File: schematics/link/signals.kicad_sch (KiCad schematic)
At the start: 39 parts, among them SW1 Feedbacks, SW2 Returns, SW3 Feedbacks, SW4 Returns, U4 AD8422ARMZ, U5 OPA2182, U6 AD8422ARMZ

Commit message: update(pcb): combining modules
Want to try a different layout, but like where I am at right now
Planning to branch off of this one and see where it goes
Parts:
- C15, C16, C17, C18, C19, C20, C21, C22, C23, C24: footprint Capacitor_SMD:C_0603_1608Metric -> Capacitor_SMD:C_0402_1005Metric
- R10, R11, R13, R14, R16, R17, R20, R21, R23, R24, R26, R27: footprint Resistor_SMD:R_0603_1608Metric -> Resistor_SMD:R_0402_1005Metric
- R12, R15, R22, R25: footprint Resistor_SMD:R_0603_1608Metric -> Resistor_SMD:R_0402_1005Metric_Pad0.72x0.64mm_HandSolder
- TP10, TP11: footprint TestPoint:TestPoint_Pad_D1.0mm -> Link_Footprints:TestPoint_Pad_D1.5mm
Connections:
- net GND: now also U5.3 (+), U5.5 (+); no longer U5.3 (+), U5.5 (+)
- net Sc1-: now also U5.7; no longer U5.1
- net Sc2-: now also U5.1; no longer U5.7
- net at C21.1, R27.2: now also U5.2 (-); no longer U5.6 (-)
- net at C22.2, R23.2, R24.2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: no longer TP11.1
- net at C18.2, R13.2, R14.2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: no longer TP10.1
- net at C17.1, R17.2: now also U5.6 (-); no longer U5.2 (-)
- net at SW3.1, SW3.2, SW3.3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: now also TP11.1
- net at SW1.1, SW1.2, SW1.3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: now also TP10.1
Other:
- moved on the sheet: TP10, TP11
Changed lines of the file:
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@@
 	)
 	(junction
-		(at 137.16 53.34)
+		(at 85.09 53.34)
 		(diameter 0)
 		(color 0 0 0 0)
 	)
 	(junction
-		(at 128.27 116.84)
+		(at 137.16 53.34)
 		(diameter 0)
 		(color 0 0 0 0)
 	)
 	(junction
-		(at 128.27 50.8)
+		(at 128.27 116.84)
 		(diameter 0)
 		(color 0 0 0 0)
@@
 	)
 	(junction
-		(at 128.27 114.3)
+		(at 92.71 53.34)
 		(diameter 0)
 		(color 0 0 0 0)
 	)
 	(junction
-		(at 92.71 53.34)
+		(at 137.16 116.84)
 		(diameter 0)
 		(color 0 0 0 0)
 	)
 	(junction
-		(at 137.16 116.84)
+		(at 85.09 116.84)
 		(diameter 0)
 		(color 0 0 0 0)
@@
 	(wire
 		(pts
+			(xy 85.09 116.84) (xy 92.71 116.84)
+		)
+		(stroke
+			(width 0)
+			(type default)
+		)
+	)
+	(wire
+		(pts
 			(xy 40.64 77.47) (xy 40.64 80.01)
 		)
@@
 	(wire
 		(pts
-			(xy 83.82 53.34) (xy 92.71 53.34)
+			(xy 83.82 53.34) (xy 85.09 53.34)
 		)
 		(stroke
@@
 	(wire
 		(pts
+			(xy 85.09 53.34) (xy 92.71 53.34)
+		)
+		(stroke
+			(width 0)
+			(type default)
+		)
+	)
+	(wire
+		(pts
 			(xy 241.3 45.72) (xy 247.65 45.72)
 		)
@@
 	(wire
 		(pts
-			(xy 83.82 116.84) (xy 92.71 116.84)
+			(xy 83.82 116.84) (xy 85.09 116.84)
 		)
 		(stroke
@@
 			)
 		)
-		(property "Footprint" "Capacitor_SMD:C_0603_1608Metric"
+		(property "Footprint" "Capacitor_SMD:C_0402_1005Metric"
 			(at 241.3 67.31 0)
 			(hide yes)
@@
 			)
 		)
-		(property "Footprint" "Resistor_SMD:R_0603_1608Metric"
+		(property "Footprint" "Resistor_SMD:R_0402_1005Metric_Pad0.72x0.64mm_HandSolder"
 			(at 60.96 116.84 0)
 			(hide yes)
@@
 		(at 156.21 119.38 0)
 		(mirror x)
-		(unit 2)
+		(unit 1)
 		(body_style 1)
 		(exclude_from_sim no)
@@
 				(path "/e6a73b1b-9233-47b9-8d6b-253608bed688/8a1af58c-1394-41ad-9137-7f60a6d007c9"
 					(reference "U5")
-					(unit 2)
+					(unit 1)
 				)
 			)
@@
 	(symbol
 		(lib_id "Connector:TestPoint")
-		(at 128.27 114.3 0)
+		(at 85.09 116.84 180)
 		(unit 1)
 		(body_style 1)
@@
 		(dnp no)
 		(property "Reference" "TP11"
-			(at 128.27 108.204 0)
+			(at 85.09 122.936 0)
 			(show_name no)
 			(do_not_autoplace no)
@@
 		)
 		(property "Value" "S2"
-			(at 128.27 106.426 0)
+			(at 85.09 124.714 0)
 			(show_name no)
 			(do_not_autoplace no)
@@
 			)
 		)
-		(property "Footprint" "TestPoint:TestPoint_Pad_D1.0mm"
-			(at 133.35 114.3 0)
+		(property "Footprint" "Link_Footprints:TestPoint_Pad_D1.5mm"
+			(at 80.01 116.84 0)
 			(hide yes)
 			(show_name no)
@@
 		)
 		(property "Datasheet" ""
-			(at 133.35 114.3 0)
+			(at 80.01 116.84 0)
 			(hide yes)
 			(show_name no)
@@
 		)
 		(property "Description" "test point"
-			(at 128.27 114.3 0)
+			(at 85.09 116.84 0)
 			(hide yes)
 			(show_name no)
@@
 		)
 		(property "FT Rotation Offset" ""
-			(at 128.27 114.3 0)
+			(at 85.09 116.84 0)
 			(hide yes)
 			(show_name no)
@@
 		)
 		(property "Sim.Params" ""
-			(at 128.27 114.3 0)
+			(at 85.09 116.84 0)
 			(hide yes)
 			(show_name no)
@@
 			)
 		)
-		(property "Footprint" "Resistor_SMD:R_0603_1608Metric"
+		(property "Footprint" "Resistor_SMD:R_0402_1005Metric"
 			(at 113.03 50.8 0)
 			(hide yes)
@@
 			)
 		)
-		(property "Footprint" "Capacitor_SMD:C_0603_1608Metric"
+		(property "Footprint" "Capacitor_SMD:C_0402_1005Metric"
 			(at 241.3 49.53 0)
 			(hide yes)
@@
 			)
 		)
-		(property "Footprint" "Resistor_SMD:R_0603_1608Metric"
+		(property "Footprint" "Resistor_SMD:R_0402_1005Metric"
 			(at 142.24 53.34 0)
 			(hide yes)
@@
 			)
 		)
-		(property "Footprint" "Capacitor_SMD:C_0603_1608Metric"
+		(property "Footprint" "Capacitor_SMD:C_0402_1005Metric"
 			(at 67.31 38.1 0)
 			(hide yes)
@@
 			)
 		)
-		(property "Footprint" "Resistor_SMD:R_0603_1608Metric"
+		(property "Footprint" "Resistor_SMD:R_0402_1005Metric"
 			(at 142.24 116.84 0)
 			(hide yes)
@@
 			)
 		)
-		(property "Footprint" "Capacitor_SMD:C_0603_1608Metric"
+		(property "Footprint" "Capacitor_SMD:C_0402_1005Metric"
 			(at 64.77 66.04 0)
 			(hide yes)
@@
 			)
 		)
-		(property "Footprint" "Resistor_SMD:R_0603_1608Metric"
+		(property "Footprint" "Resistor_SMD:R_0402_1005Metric"
 			(at 113.03 53.34 0)
 			(hide yes)
@@
 			)
 		)
-		(property "Footprint" "Resistor_SMD:R_0603_1608Metric"
+		(property "Footprint" "Resistor_SMD:R_0402_1005Metric_Pad0.72x0.64mm_HandSolder"
 			(at 60.96 53.34 0)
 			(hide yes)
@@
 	(symbol
 		(lib_id "Connector:TestPoint")
-		(at 128.27 50.8 0)
+		(at 85.09 53.34 180)
 		(unit 1)
 		(body_style 1)
@@
 		(dnp no)
 		(property "Reference" "TP10"
-			(at 128.27 44.704 0)
+			(at 85.09 59.436 0)
 			(show_name no)
 			(do_not_autoplace no)
@@
 		)
 		(property "Value" "S1"
-			(at 128.27 42.926 0)
+			(at 85.09 61.214 0)
 			(show_name no)
 			(do_not_autoplace no)
@@
 			)
 		)
-		(property "Footprint" "TestPoint:TestPoint_Pad_D1.0mm"
-			(at 133.35 50.8 0)
+		(property "Footprint" "Link_Footprints:TestPoint_Pad_D1.5mm"
+			(at 80.01 53.34 0)
 			(hide yes)
 			(show_name no)
@@
 		)
 		(property "Datasheet" ""
-			(at 133.35 50.8 0)
+			(at 80.01 53.34 0)
 			(hide yes)
 			(show_name no)
@@
 		)
 		(property "Description" "test point"
-			(at 128.27 50.8 0)
+			(at 85.09 53.34 0)
 			(hide yes)
 			(show_name no)
@@
 		)
 		(property "FT Rotation Offset" ""
-			(at 128.27 50.8 0)
+			(at 85.09 53.34 0)
 			(hide yes)
 			(show_name no)
@@
 		)
 		(property "Sim.Params" ""
-			(at 128.27 50.8 0)
+			(at 85.09 53.34 0)
 			(hide yes)
 			(show_name no)
@@
 			)
 		)
-		(property "Footprint" "Capacitor_SMD:C_0603_1608Metric"
+		(property "Footprint" "Capacitor_SMD:C_0402_1005Metric"
 			(at 64.77 129.54 0)
 			(hide yes)
@@
 			)
 		)
-		(property "Footprint" "Resistor_SMD:R_0603_1608Metric"
+		(property "Footprint" "Resistor_SMD:R_0402_1005Metric"
 			(at 113.03 116.84 0)
 			(hide yes)
@@
 		(at 156.21 55.88 0)
 		(mirror x)
-		(unit 1)
+		(unit 2)
 		(body_style 1)
 		(exclude_from_sim no)
@@
 				(path "/e6a73b1b-9233-47b9-8d6b-253608bed688/8a1af58c-1394-41ad-9137-7f60a6d007c9"
 					(reference "U5")
-					(unit 1)
+					(unit 2)
 				)
 			)
@@
 			)
 		)
-		(property "Footprint" "Capacitor_SMD:C_0603_1608Metric"
+		(property "Footprint" "Capacitor_SMD:C_0402_1005Metric"
 			(at 137.16 121.92 0)
 			(hide yes)
@@
 			)
 		)
-		(property "Footprint" "Resistor_SMD:R_0603_1608Metric"
+		(property "Footprint" "Resistor_SMD:R_0402_1005Metric"
 			(at 154.94 33.02 0)
 			(hide yes)
@@
 			)
 		)
-		(property "Footprint" "Capacitor_SMD:C_0603_1608Metric"
+		(property "Footprint" "Capacitor_SMD:C_0402_1005Metric"
 			(at 154.94 106.68 0)
 			(hide yes)
@@
 			)
 		)
-		(property "Footprint" "Resistor_SMD:R_0603_1608Metric"
+		(property "Footprint" "Resistor_SMD:R_0402_1005Metric_Pad0.72x0.64mm_HandSolder"
 			(at 113.03 55.88 0)
 			(hide yes)
@@
 			)
 		)
-		(property "Footprint" "Capacitor_SMD:C_0603_1608Metric"
+		(property "Footprint" "Capacitor_SMD:C_0402_1005Metric"
 			(at 154.94 43.18 0)
 			(hide yes)
@@
 			)
 		)
-		(property "Footprint" "Resistor_SMD:R_0603_1608Metric"
+		(property "Footprint" "Resistor_SMD:R_0402_1005Metric"
 			(at 24.13 48.26 0)
 			(hide yes)
@@
 			)
 		)
-		(property "Footprint" "Resistor_SMD:R_0603_1608Metric"
+		(property "Footprint" "Resistor_SMD:R_0402_1005Metric"
 			(at 154.94 96.52 0)
 			(hide yes)
@@
 			)
 		)
-		(property "Footprint" "Resistor_SMD:R_0603_1608Metric"
+		(property "Footprint" "Resistor_SMD:R_0402_1005Metric"
 			(at 24.13 58.42 0)
 			(hide yes)
@@
 			)
 		)
-		(property "Footprint" "Resistor_SMD:R_0603_1608Metric"
+		(property "Footprint" "Resistor_SMD:R_0402_1005Metric_Pad0.72x0.64mm_HandSolder"
 			(at 113.03 119.38 0)
 			(hide yes)
@@
 			)
 		)
-		(property "Footprint" "Resistor_SMD:R_0603_1608Metric"
+		(property "Footprint" "Resistor_SMD:R_0402_1005Metric"
 			(at 24.13 111.76 0)
 			(hide yes)
@@
 			)
 		)
-		(property "Footprint" "Resistor_SMD:R_0603_1608Metric"
+		(property "Footprint" "Resistor_SMD:R_0402_1005Metric"
 			(at 24.13 121.92 0)
 			(hide yes)
@@
 			)
 		)
-		(property "Footprint" "Resistor_SMD:R_0603_1608Metric"
+		(property "Footprint" "Resistor_SMD:R_0402_1005Metric"
 			(at 113.03 114.3 0)
 			(hide yes)
@@
 			)
 		)
-		(property "Footprint" "Capacitor_SMD:C_0603_1608Metric"
+		(property "Footprint" "Capacitor_SMD:C_0402_1005Metric"
 			(at 137.16 58.42 0)
 			(hide yes)
@@
 			)
 		)
-		(property "Footprint" "Capacitor_SMD:C_0603_1608Metric"
+		(property "Footprint" "Capacitor_SMD:C_0402_1005Metric"
 			(at 67.31 101.6 0)
 			(hide yes)

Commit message: update(link): finalized placements
Still some work to be done:
1. Fix planes under RJ45 connector, probably should keep out if possible
2. Fix silkscreening
3. Fix isolated filled zones
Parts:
- TP10: value S1 -> S2
- TP11: value S2 -> S1
- renumbered C15 to C17, C17 to C18, C23 to C19, C18 to C20, C16 to C21, C24 to C22, C19 to C23, C21 to C24, C22 to C25, C20 to C26, R16 to R10, R10 to R11, R13 to R12, R12 to R13, R17 to R15, R15 to R16, R11 to R17, R26 to R20, R20 to R21, R23 to R22, R22 to R23, R27 to R25, R25 to R26, R21 to R27
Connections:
- net S1+: now also R27.1; no longer R17.1
- net S1-: now also R21.1; no longer R11.1
- net S2+: now also R17.1; no longer R27.1
- net S2-: now also R11.1; no longer R21.1
- net Sc1-: now also C24.2, R20.2, U5.1; no longer C18.2, R10.2, U5.7
- net Sc2-: now also C18.2, R10.2, U5.7; no longer C24.2, R20.2, U5.1

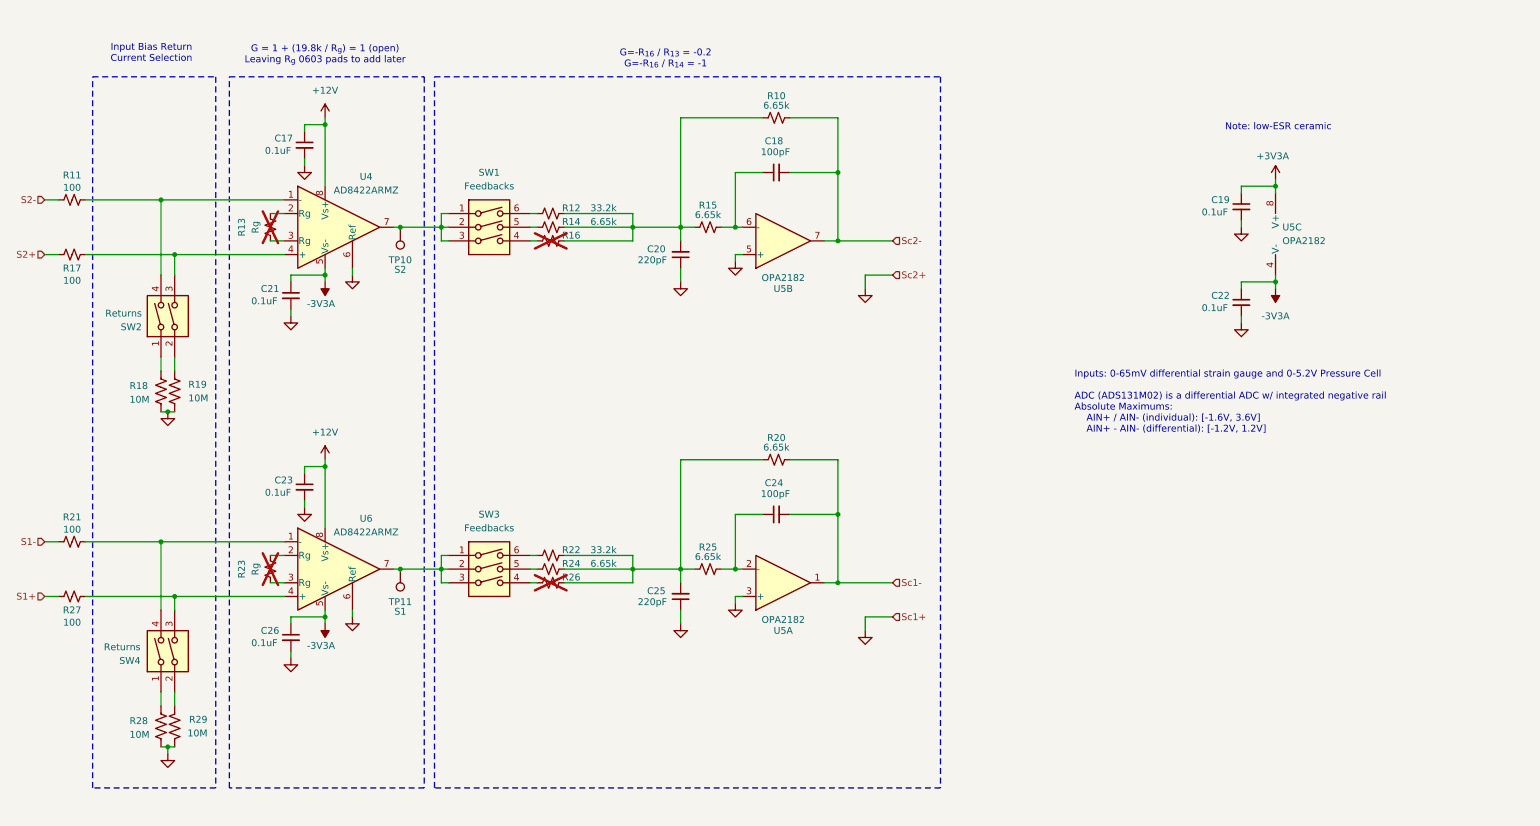
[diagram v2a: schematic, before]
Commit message: update(review):
1. Take gain resistor out of AFE filter
2. Breakout I2C
3. Move fuse to cover both 12V rails
4. Silkscreens
5. More testpoints + change to clip ons
6. Match ADC input max and filter output max
7. Add shunt for current resistors
8. Thermocouples
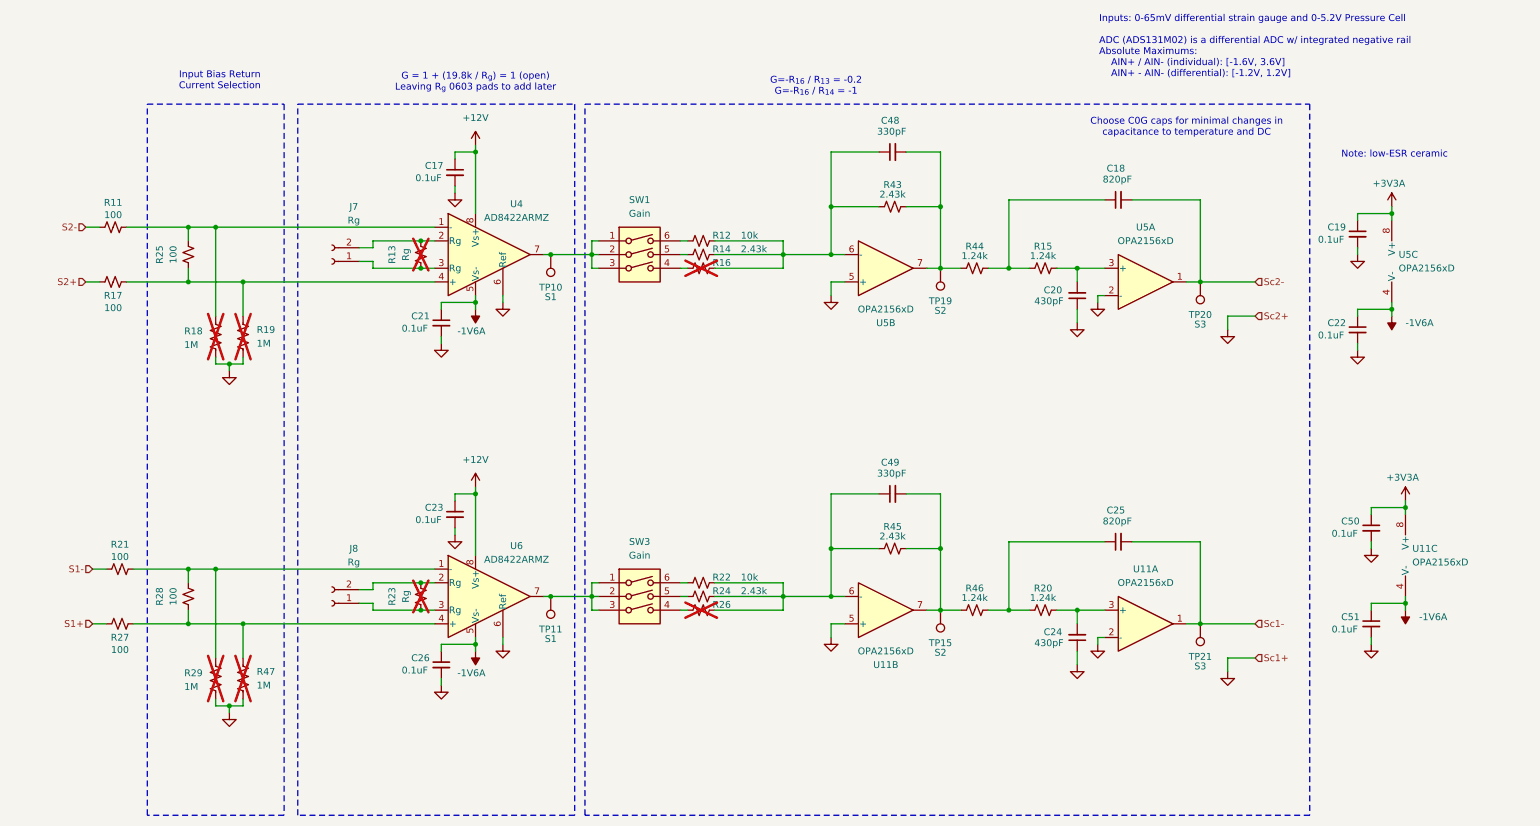
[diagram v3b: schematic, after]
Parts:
- removed R10: 6.65k, Resistor_SMD:R_0402_1005Metric, symbol Device:R_Small_US
- removed R28: 10M, Resistor_SMD:R_0603_1608Metric, symbol Device:R_US
- removed SW2, SW4: Returns, Button_Switch_SMD:SW_DIP_SPSTx02_Slide_KingTek_DSHP02TJ_W5.25mm_P1.27mm_JPin, symbol Switch:SW_DIP_x02
- removed U5: OPA2182, Link_Footprints:OPA2182, symbol Link_Components:OPA2182
- added C48, C49: 330pF, Capacitor_SMD:C_0402_1005Metric, symbol Device:C_Small
- added C50, C51: 0.1uF, Capacitor_SMD:C_0402_1005Metric, symbol Device:C_Small
- added J7, J8: Rg, Connector_PinSocket_2.54mm:PinSocket_1x02_P2.54mm_Vertical, symbol Connector:Conn_01x02_Socket
- added R28: 100, Connector_PinSocket_2.54mm:PinSocket_1x02_P2.54mm_Vertical, symbol Device:R_Small_US
- added R43, R45: 2.43k, Resistor_SMD:R_0402_1005Metric, symbol Device:R_Small_US
- added R44, R46: 1.24k, Resistor_SMD:R_0402_1005Metric, symbol Device:R_Small_US
- added R47: 1M, Resistor_SMD:R_0603_1608Metric_Pad0.98x0.95mm_HandSolder, symbol Device:R_US
- added TP15, TP19: S2, Link_Footprints:Keystone5001, symbol Connector:TestPoint
- added TP20, TP21: S3, Link_Footprints:Keystone5001, symbol Connector:TestPoint
- added U11, U5: OPA2156xD, Package_SO:SOIC-8_3.9x4.9mm_P1.27mm, symbol Amplifier_Operational:OPA2156xD
- C17, C19, C21, C22, C23, C26: MPN (none) -> GRM155R71H104KE14D
- C18: value 100pF -> 820pF; MPN (none) -> GRM1555C1H821JA01D
- C20: value 220pF -> 430pF; MPN (none) -> GCM1555C1H431FA16D
- C24: value 100pF -> 430pF; MPN (none) -> GCM1555C1H431FA16D
- C25: value 220pF -> 820pF; MPN (none) -> GRM1555C1H821JA01D
- R11, R17, R21, R27: MPN (none) -> RT0402BRD07100RL
- R12, R22: value 33.2k -> 10k; MPN (none) -> RT0402BRD0710KL
- R13, R23: MPN (none) -> N/A
- R14, R24: value 6.65k -> 2.43k; MPN (none) -> RT0402FRE072K43L
- R15, R20: value 6.65k -> 1.24k; MPN (none) -> RT0402BRD071K24L
- R16, R26: MPN (none) -> N/A; now left out of the parts list
- R18, R19: value 10M -> 1M; footprint Resistor_SMD:R_0603_1608Metric -> Resistor_SMD:R_0603_1608Metric_Pad0.98x0.95mm_HandSolder; MPN (none) -> RC0603FR-071ML; now not fitted; now left out of the parts list
- R25: value 6.65k -> 100; footprint Resistor_SMD:R_0402_1005Metric -> Connector_PinSocket_2.54mm:PinSocket_1x02_P2.54mm_Vertical; LCSC Part # C95204 -> (none); MPN (none) -> SSK02-FPH-254-A2
- R29: value 10M -> 1M; footprint Resistor_SMD:R_0603_1608Metric -> Resistor_SMD:R_0603_1608Metric_Pad0.98x0.95mm_HandSolder; LCSC Part # C7250 -> C7250; MPN (none) -> RC0603FR-071ML; now not fitted; now left out of the parts list
- SW1, SW3: value Feedbacks -> Gain; footprint Button_Switch_SMD:SW_DIP_SPSTx03_Slide_KingTek_DSHP03TJ_W5.25mm_P1.27mm_JPin -> Link_Footprints:wurth_3pos_dip; MPN (none) -> 416131160803
- TP10: value S2 -> S1; footprint Link_Footprints:TestPoint_Pad_D1.5mm -> Link_Footprints:Keystone5001; MPN (none) -> 5001; now in the parts list
- TP11: footprint Link_Footprints:TestPoint_Pad_D1.5mm -> Link_Footprints:Keystone5001; MPN (none) -> 5001; now in the parts list
- U4, U6: MPN (none) -> AD8422ARMZ
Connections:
- net +3V3A: now also C50.1, U11.8 (V+), U5.8 (V+)
- net GND: now also C24.1, C50.2, C51.2, R47.2, U11.2 (-), U11.5 (+), U5.2 (-), U5.5 (+); no longer C25.1
- net Sc1-: now also C25.2, TP21.1, U11.1; no longer C24.2, R20.2
- net Sc2-: now also TP20.1, U5.1
- net at R23.1, U6.3 (Rg): now also J8.1 (Pin_1)
- net at R23.2, U6.2 (Rg): now also J8.2 (Pin_2)
- net at R25.2: now also R11.2, R18.1, U4.1 (-); no longer C24.1
- net at R29.1: now also R21.2, U6.1 (-), R28.2
- net at R12.2, R14.2, R16.2: now also C48.1, R43.1, U5.6 (-); no longer C20.2, R15.1
- net at R27.2, U6.4 (+): now also R28.1, R47.1
- net at C18.1: now also R15.1, R44.2; no longer R15.2
- net at R22.2, R24.2, R26.2: now also C49.1, R45.1, U11.6 (-); no longer C25.2, R20.1, R25.1
- net at R13.1, U4.3 (Rg): now also J7.1 (Pin_1)
- net at R13.2, U4.2 (Rg): now also J7.2 (Pin_2)
- net at R19.1: now also R17.2, R25.1, U4.4 (+)
- net -3V3A renamed -1V6A
- net -1V6A: now also C51.1, U11.4 (V-), U5.4 (V-)
- new net: C49.2, R45.2, R46.1, TP15.1, U11.7
- new net: C24.2, R20.2, U11.3 (+)
- new net: C48.2, R43.2, R44.1, TP19.1, U5.7
- new net: C20.2, R15.2, U5.3 (+)
- new net: C25.1, R20.1, R46.2
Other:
- note added: "Choose C0G caps for minimal changes in capacitance to temperature and DC"
- moved on the sheet: C17, C18, C19, C20, C21, C22, C23, C26, R11, R12, R13, R14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

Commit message: GPT review
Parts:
- R12, R22: value 10k -> 11k; LCSC Part # C95204 -> (none); MPN RT0402BRD0710KL -> RT0402BRD0711KL
- R25, R28: value 100 -> Shunt
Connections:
- net GND: no longer U11.2 (-), U5.2 (-)
- net Sc1-: now also U11.2 (-)
- net Sc2-: now also U5.2 (-)
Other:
- note added: "Note: If used, shunt = 100"
- moved on the sheet: TP20, TP21

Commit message: GPT review pt2
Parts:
- C17, C19, C21, C22, C23, C26, C50, C51: MPN GRM155R71H104KE14D -> GCM155R71H104KE02D
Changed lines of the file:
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@@
 			)
 		)
-		(property "MPN" "GRM155R71H104KE14D"
+		(property "MPN" "GCM155R71H104KE02D"
 			(at 262.89 72.39 0)
 			(hide yes)
@@
 			)
 		)
-		(property "MPN" "GRM155R71H104KE14D"
+		(property "MPN" "GCM155R71H104KE02D"
 			(at 265.43 109.22 0)
 			(hide yes)
@@
 			)
 		)
-		(property "MPN" "GRM155R71H104KE14D"
+		(property "MPN" "GCM155R71H104KE02D"
 			(at 265.43 127 0)
 			(hide yes)
@@
 			)
 		)
-		(property "MPN" "GRM155R71H104KE14D"
+		(property "MPN" "GCM155R71H104KE02D"
 			(at 262.89 54.61 0)
 			(hide yes)
@@
 			)
 		)
-		(property "MPN" "GRM155R71H104KE14D"
+		(property "MPN" "GCM155R71H104KE02D"
 			(at 95.25 43.18 0)
 			(hide yes)
@@
 			)
 		)
-		(property "MPN" "GRM155R71H104KE14D"
+		(property "MPN" "GCM155R71H104KE02D"
 			(at 92.71 71.12 0)
 			(hide yes)
@@
 			)
 		)
-		(property "MPN" "GRM155R71H104KE14D"
+		(property "MPN" "GCM155R71H104KE02D"
 			(at 92.71 134.62 0)
 			(hide yes)
@@
 			)
 		)
-		(property "MPN" "GRM155R71H104KE14D"
+		(property "MPN" "GCM155R71H104KE02D"
 			(at 95.25 106.68 0)
 			(hide yes)
